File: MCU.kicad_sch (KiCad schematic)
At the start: 35 parts, among them J200 SWD, J201 USB_B_Micro, SW200 SW_SPDT, U200 STM32F405RGT6, U201 USBLC6-2SC6, Y200 16MHz

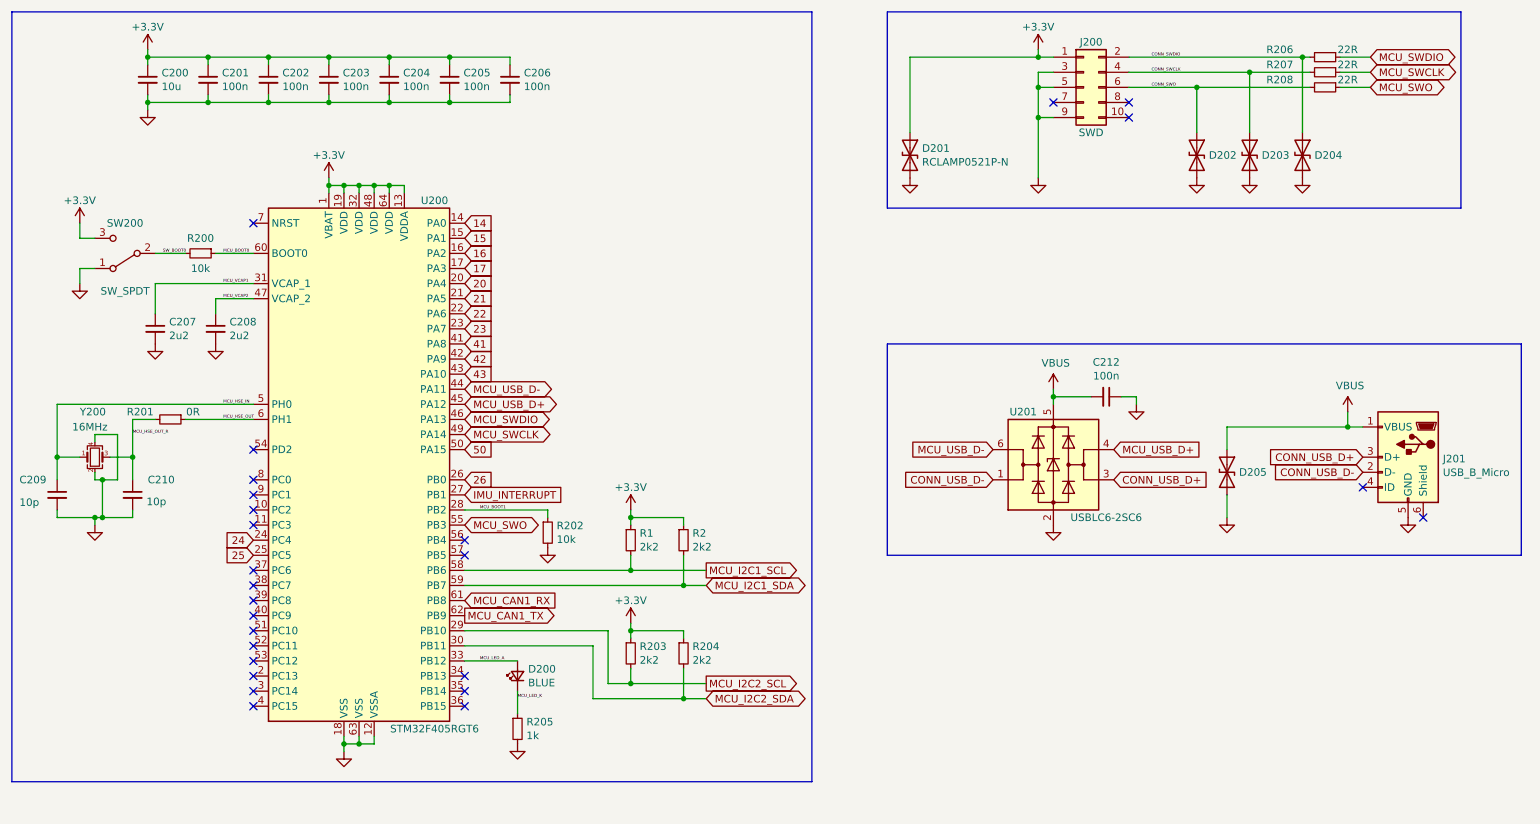
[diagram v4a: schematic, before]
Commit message: gpio breakout stuff
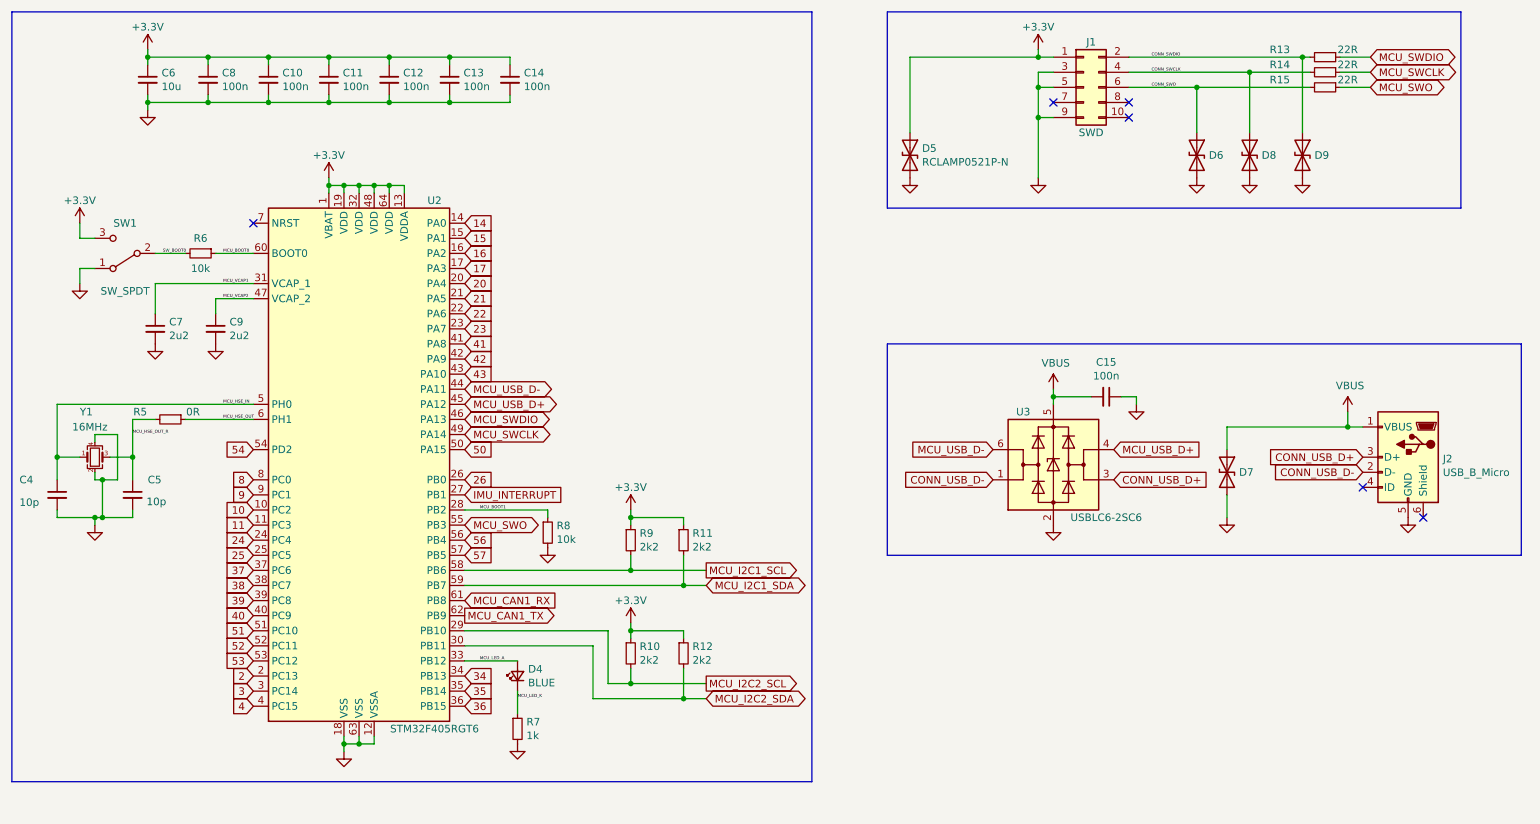
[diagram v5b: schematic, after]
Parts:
- renumbered C202 to C10, C203 to C11, C204 to C12, C205 to C13, C206 to C14, C212 to C15, C209 to C4, C210 to C5, C200 to C6, C207 to C7, C201 to C8, C208 to C9, D200 to D4, D201 to D5, D202 to D6, D205 to D7, D203 to D8, D204 to D9, J200 to J1, J201 to J2, R203 to R10, R2 to R11, R204 to R12, R206 to R13, R207 to R14, R208 to R15, R201 to R5, R200 to R6, R205 to R7, R202 to R8, R1 to R9, SW200 to SW1, U200 to U2, U201 to U3, Y200 to Y1
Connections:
- net 10: now reaches U2.10 (PC2)
- net 11: now reaches U2.11 (PC3)
- net 2: now reaches U2.2 (PC13)
- net 3: now reaches U2.3 (PC14)
- net 34: now reaches U2.34 (PB13)
- net 35: now reaches U2.35 (PB14)
- net 36: now reaches U2.36 (PB15)
- net 37: now reaches U2.37 (PC6)
- net 38: now reaches U2.38 (PC7)
- net 39: now reaches U2.39 (PC8)
- net 4: now reaches U2.4 (PC15)
- net 40: now reaches U2.40 (PC9)
- net 51: now reaches U2.51 (PC10)
- net 52: now reaches U2.52 (PC11)
- net 53: now reaches U2.53 (PC12)
- net 54: now reaches U2.54 (PD2)
- net 56: now reaches U2.56 (PB4)
- net 57: now reaches U2.57 (PB5)
- net 8: now reaches U2.8 (PC0)
- net 9: now reaches U2.9 (PC1)
- no-connect marks 26 -> 6

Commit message: sdignionsrg
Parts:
- removed J2: USB_B_Micro, BluePhil-Footprints:MicroXNJ, symbol Connector:USB_B_Micro
- added J9: 2169900003, MOLEX_2169900003, symbol USB C:2169900003
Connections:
- net CONN_USB_D+: now also J9.A6 (DP1), J9.B6 (DP2)
- net CONN_USB_D-: now also J9.A7 (DN1), J9.B7 (DN2)
- net GND: now also J9.A1_B12 (GND), J9.B1_A12 (GND)
- net VBUS: now also J9.A4_B9 (VBUS), J9.B4_A9 (VBUS)
- new net: J9.S1 (SHIELD), J9.S2 (SHIELD), J9.S3 (SHIELD), J9.S4 (SHIELD)
- no-connect marks 6 -> 9
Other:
- moved on the sheet: D7

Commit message: siobgg:
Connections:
- net CONN_USB_D+: no longer J9.A6 (DP1)
- net CONN_USB_D-: no longer J9.A7 (DN1)
- no-connect marks 9 -> 11
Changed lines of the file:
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@@
   (no_connect (at 250.19 140.97))
   (no_connect (at 66.04 78.74))
+  (no_connect (at 214.63 146.05))
+  (no_connect (at 214.63 143.51))
   (no_connect (at 250.19 148.59))
   (no_connect (at 213.36 58.42))
@@
     )
   )
-  (global_label "CONN_USB_D+" (shape input) (at 214.63 143.51 180) (fields_autoplaced)
-    (effects (font (size 1.27 1.27)) (justify right))
-    (property "Intersheet References" "${INTERSHEET_REFS}" (id 0) (at -38.1 25.4 0)
-      (effects (font (size 1.27 1.27)) hide)
-    )
-  )
   (global_label "MCU_SWO" (shape bidirectional) (at 101.6 129.54 0) (fields_autoplaced)
     (effects (font (size 1.27 1.27)) (justify left))
@@
       (effects (font (size 1.27 1.27)) hide)
     )
-  )
-  (global_label "CONN_USB_D-" (shape input) (at 214.63 146.05 180) (fields_autoplaced)
-    (effects (font (size 1.27 1.27)) (justify right))
-    (property "Intersheet References" "${INTERSHEET_REFS}" (id 0) (at -38.1 25.4 0)
-      (effects (font (size 1.27 1.27)) hide)
-    )

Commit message: WEBGIOWEBGIOBWEG
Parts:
- removed D4: BLUE, LED_SMD:LED_0603_1608Metric, symbol Device:LED_Small
- removed D7: RCLAMP0521P-N, Diode_SMD:D_0402_1005Metric, symbol Device:D_TVS
- removed J9: 2169900003, MOLEX_2169900003, symbol USB C:2169900003
- removed R7: 1k, Resistor_SMD:R_0402_1005Metric, symbol Device:R_Small
- added D301: BLUE, LED_SMD:LED_0603_1608Metric, symbol Device:LED_Small
- added D306: RCLAMP0521P-N, Diode_SMD:D_0402_1005Metric, symbol Device:D_TVS
- added J302: USB_C_Receptacle_USB2.0, Connector_USB:USB_C_Receptacle_XKB_U262-16XN-4BVC11, symbol Connector:USB_C_Receptacle_USB2.0
- added R303: 1k, Resistor_SMD:R_0402_1005Metric, symbol Device:R_Small
- added R312, R313: 2k2, Resistor_SMD:R_0402_1005Metric, symbol Device:R_Small
- renumbered C4 to C301, C5 to C302, C6 to C303, C7 to C304, C8 to C305, C9 to C306, C10 to C307, C11 to C308, C12 to C309, C13 to C310, C14 to C311, C15 to C312, D5 to D302, D6 to D303, D8 to D304, D9 to D305, J1 to J301, R5 to R301, R6 to R302, R8 to R304, R9 to R305, R10 to R306, R11 to R307, R12 to R308, R13 to R309, R14 to R310, R15 to R311, SW1 to SW301, U2 to U301, U3 to U302, Y1 to Y301
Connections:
- net 36 is gone; now on net MCU_LED_A: U301.36 (PB15)
- net CONN_USB_D+: now also J302.A6 (D+), J302.B6 (D+)
- net CONN_USB_D-: now also J302.A7 (D-), J302.B7 (D-)
- net GND: now also D306.2 (A2), J302.A1 (GND), J302.A12 (GND), J302.B1 (GND), J302.B12 (GND), J302.S1 (SHIELD), R303.2, R312.2, R313.2
- net MCU_LED_A: now also D301.2 (A); no longer U301.33 (PB12)
- net MCU_LED_K: now also D301.1 (K), R303.1
- net VBUS: now also D306.1 (A1), J302.A4 (VBUS), J302.A9 (VBUS), J302.B4 (VBUS), J302.B9 (VBUS)
- net 14 renamed MCU_TXD
- net 15 renamed MCU_RXD
- new net: J302.A5 (CC1), R312.1
- new net: J302.B5 (CC2), R313.1
- new net 33: U301.33 (PB12)
- no-connect marks 11 -> 7
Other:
- note added: "SWD"
- note added: "USB C"
- moved on the sheet: C312, U302
